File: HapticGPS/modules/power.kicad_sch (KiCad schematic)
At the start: 16 parts, among them U1 NPM1300

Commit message: save
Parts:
- C3: footprint Capacitor_SMD:C_0603_1608Metric -> Capacitor_SMD:C_0402_1005Metric; Number Part GRM188Z71E225ME43D -> GRM155Z71A225KE44D; Voltage 25VDC -> 10V
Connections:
- net SW1_NPM: now reaches L1.1, U1.3 (SW1)
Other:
- moved on the sheet: C1, L1
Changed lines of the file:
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@@
 	)
 	(junction
-		(at 190.5 66.04)
+		(at 196.85 66.04)
 		(diameter 0)
 		(color 0 0 0 0)
@@
 	)
 	(junction
-		(at 180.34 66.04)
+		(at 186.69 66.04)
 		(diameter 0)
 		(color 0 0 0 0)
@@
 	)
 	(junction
-		(at 190.5 78.74)
+		(at 196.85 78.74)
 		(diameter 0)
 		(color 0 0 0 0)
@@
 	(wire
 		(pts
-			(xy 190.5 78.74) (xy 167.64 78.74)
-		)
-		(stroke
-			(width 0)
-			(type default)
-		)
-	)
-	(wire
-		(pts
-			(xy 190.5 66.04) (xy 198.12 66.04)
+			(xy 196.85 66.04) (xy 204.47 66.04)
 		)
 		(stroke
@@
 	(wire
 		(pts
-			(xy 190.5 66.04) (xy 190.5 68.58)
+			(xy 196.85 66.04) (xy 196.85 68.58)
 		)
 		(stroke
@@
 	(wire
 		(pts
+			(xy 167.64 78.74) (xy 196.85 78.74)
+		)
+		(stroke
+			(width 0)
+			(type default)
+		)
+	)
+	(wire
+		(pts
 			(xy 96.52 134.62) (xy 102.87 134.62)
 		)
@@
 	(wire
 		(pts
+			(xy 167.64 66.04) (xy 186.69 66.04)
+		)
+		(stroke
+			(width 0)
+			(type default)
+		)
+	)
+	(wire
+		(pts
 			(xy 115.57 68.58) (xy 127 68.58)
 		)
@@
 	(wire
 		(pts
-			(xy 167.64 76.2) (xy 172.72 76.2)
+			(xy 167.64 76.2) (xy 179.07 76.2)
 		)
 		(stroke
@@
 	(wire
 		(pts
-			(xy 190.5 76.2) (xy 190.5 78.74)
+			(xy 196.85 76.2) (xy 196.85 78.74)
 		)
 		(stroke
@@
 	(wire
 		(pts
-			(xy 180.34 66.04) (xy 190.5 66.04)
+			(xy 186.69 66.04) (xy 196.85 66.04)
 		)
 		(stroke
@@
 	(wire
 		(pts
-			(xy 180.34 66.04) (xy 180.34 76.2)
+			(xy 186.69 66.04) (xy 186.69 76.2)
 		)
 		(stroke
@@
 	(wire
 		(pts
-			(xy 167.64 66.04) (xy 180.34 66.04)
-		)
-		(stroke
-			(width 0)
-			(type default)
-		)
-	)
-	(wire
-		(pts
 			(xy 50.8 53.34) (xy 50.8 48.26)
 		)
@@
 		)
 	)
+	(label "SW1_NPM"
+		(at 167.64 76.2 0)
+		(effects
+			(font
+				(size 1.27 1.27)
+			)
+			(justify left bottom)
+		)
+	)
 	(label "CC2"
 		(at 115.57 44.45 0)
@@
 	(hierarchical_label "BUCK1"
 		(shape output)
-		(at 198.12 66.04 0)
+		(at 204.47 66.04 0)
 		(effects
 			(font
@@
 	(symbol
 		(lib_id "Device:L")
-		(at 176.53 76.2 90)
+		(at 182.88 76.2 90)
 		(unit 1)
 		(exclude_from_sim no)
@@
 		(dnp no)
 		(property "Reference" "L1"
-			(at 176.53 77.47 90)
+			(at 182.88 77.47 90)
 			(effects
 				(font
@@
 		)
 		(property "Value" "2.2uF"
-			(at 176.784 74.168 90)
+			(at 183.134 74.168 90)
 			(effects
 				(font
@@
 		)
 		(property "Footprint" "Inductor_SMD:L_1008_2520Metric"
-			(at 176.53 76.2 0)
+			(at 182.88 76.2 0)
 			(effects
 				(font
@@
 		)
 		(property "Datasheet" "https://mm.digikey.com/Volume0/opasdata/d220001/medias/docus/2542/CIGT252008LM2R2MNE_Spec.pdf"
-			(at 176.53 76.2 0)
+			(at 182.88 76.2 0)
 			(effects
 				(font
@@
 		)
 		(property "Description" "FIXED IND 2.2UH 2A 97 MOHM SMD"
-			(at 176.53 76.2 0)
+			(at 182.88 76.2 0)
 			(effects
 				(font
@@
 		)
 		(property "Manufacturer" "Samsung Electro-Mechanics"
-			(at 176.53 76.2 90)
+			(at 182.88 76.2 90)
 			(effects
 				(font
@@
 		)
 		(property "Number Part" "CIGT252008LM2R2MNE"
-			(at 176.53 76.2 90)
+			(at 182.88 76.2 90)
 			(effects
 				(font
@@
 		)
 		(property "Provider" "Digikey"
-			(at 176.53 76.2 90)
+			(at 182.88 76.2 90)
 			(effects
 				(font
@@
 		)
 		(property "Revisado" "REV"
-			(at 176.53 71.882 90)
+			(at 182.88 71.882 90)
 			(effects
 				(font
@@
 		)
 		(property "Voltage" ""
-			(at 176.53 76.2 0)
+			(at 182.88 76.2 0)
 			(effects
 				(font
@@
 	(symbol
 		(lib_id "power:GND")
-		(at 190.5 78.74 0)
+		(at 196.85 78.74 0)
 		(unit 1)
 		(exclude_from_sim no)
@@
 		(fields_autoplaced yes)
 		(property "Reference" "#PWR07"
-			(at 190.5 85.09 0)
+			(at 196.85 85.09 0)
 			(effects
 				(font
@@
 		)
 		(property "Value" "GND"
-			(at 190.5 83.82 0)
+			(at 196.85 83.82 0)
 			(effects
 				(font
@@
 		)
 		(property "Footprint" ""
-			(at 190.5 78.74 0)
+			(at 196.85 78.74 0)
 			(effects
 				(font
@@
 		)
 		(property "Datasheet" ""
-			(at 190.5 78.74 0)
+			(at 196.85 78.74 0)
 			(effects
 				(font
@@
 		)
 		(property "Description" "Power symbol creates a global label with name \"GND\" , ground"
-			(at 190.5 78.74 0)
+			(at 196.85 78.74 0)
 			(effects
 				(font
@@
 			)
 		)
-		(property "Footprint" "Capacitor_SMD:C_0603_1608Metric"
+		(property "Footprint" "Capacitor_SMD:C_0402_1005Metric"
 			(at 102.5652 49.53 0)
 			(effects
@@
 			)
 		)
-		(property "Datasheet" "https://search.murata.co.jp/Ceramy/image/img/A01X/G101/ENG/GRM188Z71E225ME43-01.pdf"
+		(property "Datasheet" "https://search.murata.co.jp/Ceramy/image/img/A01X/G101/ENG/GRM155Z71A225KE44-01A.pdf"
 			(at 101.6 45.72 0)
 			(effects
@@
 			)
 		)
-		(property "Description" "CAP CER 2.2UF 25V X7R 0603"
+		(property "Description" "CAP CER 2.2UF 10V X7R 0402"
 			(at 101.6 45.72 0)
 			(effects
@@
 			)
 		)
-		(property "Number Part" "GRM188Z71E225ME43D"
+		(property "Number Part" "GRM155Z71A225KE44D"
 			(at 101.6 45.72 0)
 			(effects
@@
 			)
 		)
-		(property "Voltage" "25VDC"
-			(at 108.458 49.276 0)
+		(property "Voltage" "10V"
+			(at 107.442 49.276 0)
 			(effects
 				(font
@@
 	(symbol
 		(lib_id "Device:C")
-		(at 190.5 72.39 0)
+		(at 196.85 72.39 0)
 		(unit 1)
 		(exclude_from_sim no)
@@
 		(dnp no)
 		(property "Reference" "C1"
-			(at 194.31 71.1199 0)
+			(at 200.66 71.1199 0)
 			(effects
 				(font
@@
 		)
 		(property "Value" "10uF"
-			(at 194.31 73.6599 0)
+			(at 200.66 73.6599 0)
 			(effects
 				(font
@@
 		)
 		(property "Footprint" "Capacitor_SMD:C_0603_1608Metric"
-			(at 191.4652 76.2 0)
+			(at 197.8152 76.2 0)
 			(effects
 				(font
@@
 		)
 		(property "Datasheet" "https://search.murata.co.jp/Ceramy/image/img/A01X/G101/ENG/GRM188Z71A106KA73-01A.pdf"
-			(at 190.5 72.39 0)
+			(at 196.85 72.39 0)
 			(effects
 				(font
@@
 		)
 		(property "Description" "CAP CER 10UF 10V X7R 0603"
-			(at 190.5 72.39 0)
+			(at 196.85 72.39 0)
 			(effects
 				(font
@@
 		)
 		(property "Manufacturer" "Murata Electronics"
-			(at 190.5 72.39 0)
+			(at 196.85 72.39 0)
 			(effects
 				(font
@@
 		)
 		(property "Number Part" "GRM188Z71A106KA73D"
-			(at 190.5 72.39 0)
+			(at 196.85 72.39 0)
 			(effects
 				(font
@@
 		)
 		(property "Provider" "Digikey"
-			(at 190.5 72.39 0)
+			(at 196.85 72.39 0)
 			(effects
 				(font
@@
 		)
 		(property "Voltage" "10V"
-			(at 196.088 75.946 0)
+			(at 202.438 75.946 0)
 			(effects
 				(font
@@
 		)
 		(property "Revisado" "REV"
-			(at 196.088 78.232 0)
+			(at 202.438 78.232 0)
 			(effects
 				(font

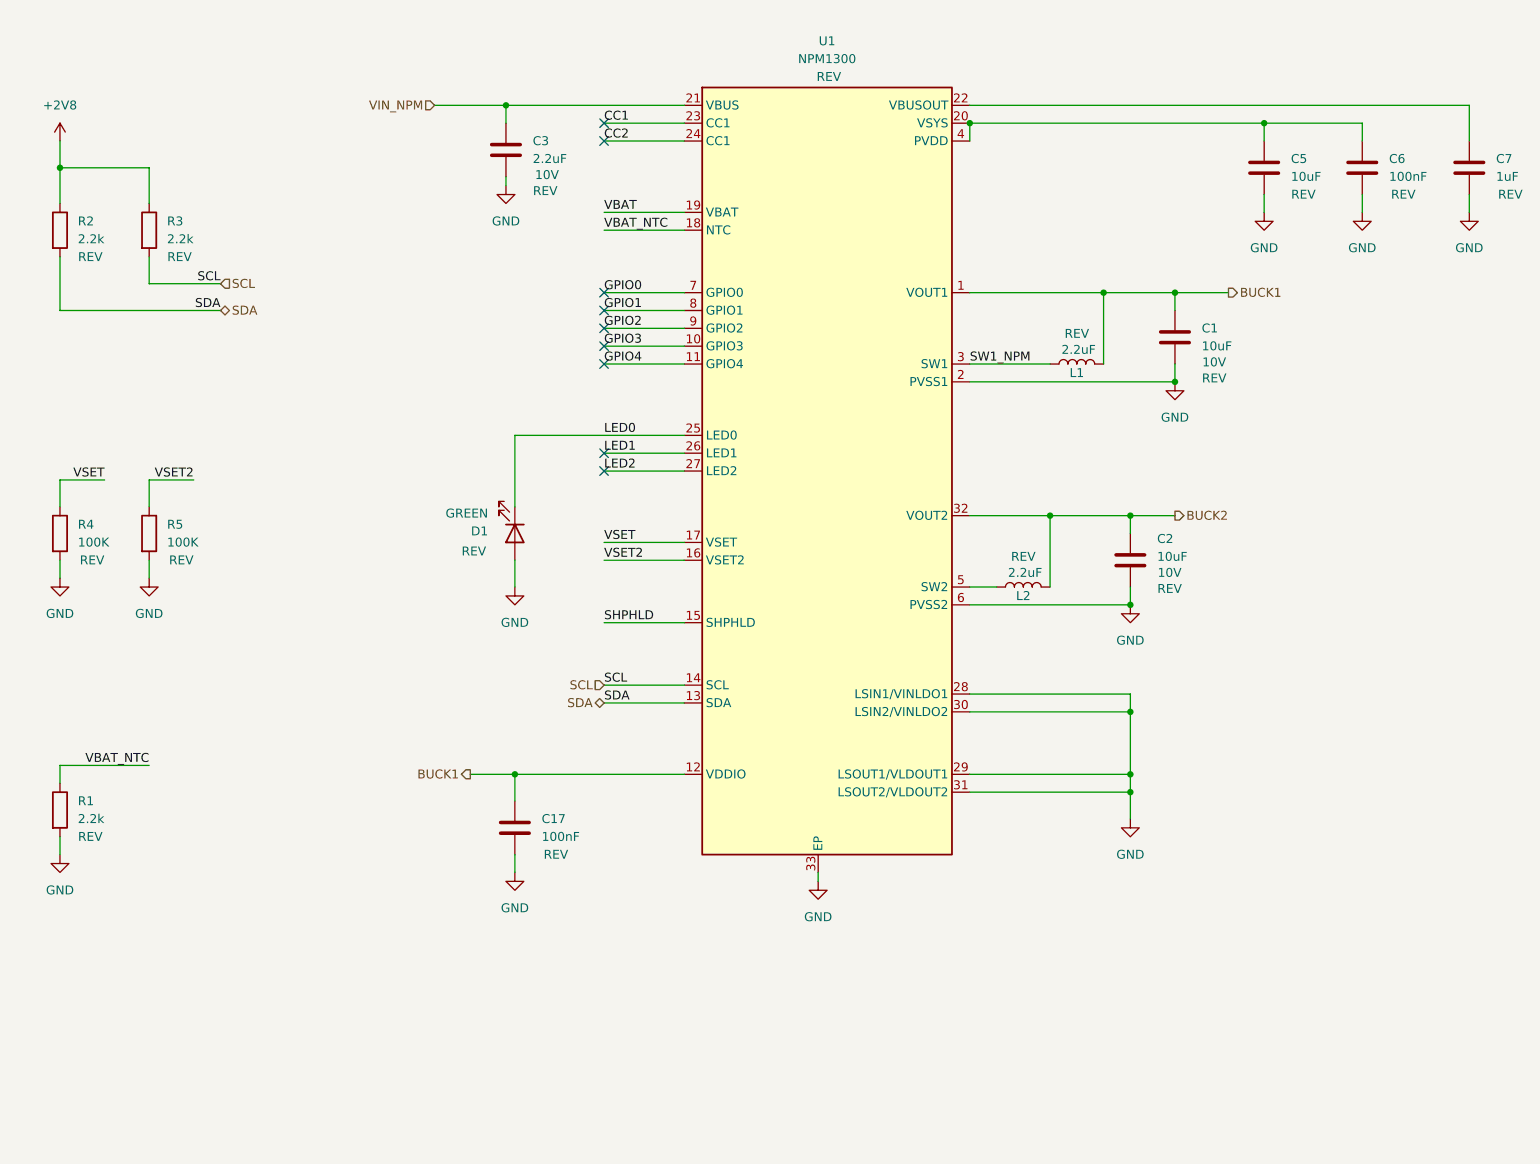
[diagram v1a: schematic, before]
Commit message: eliminating GPS, and second piezo driver
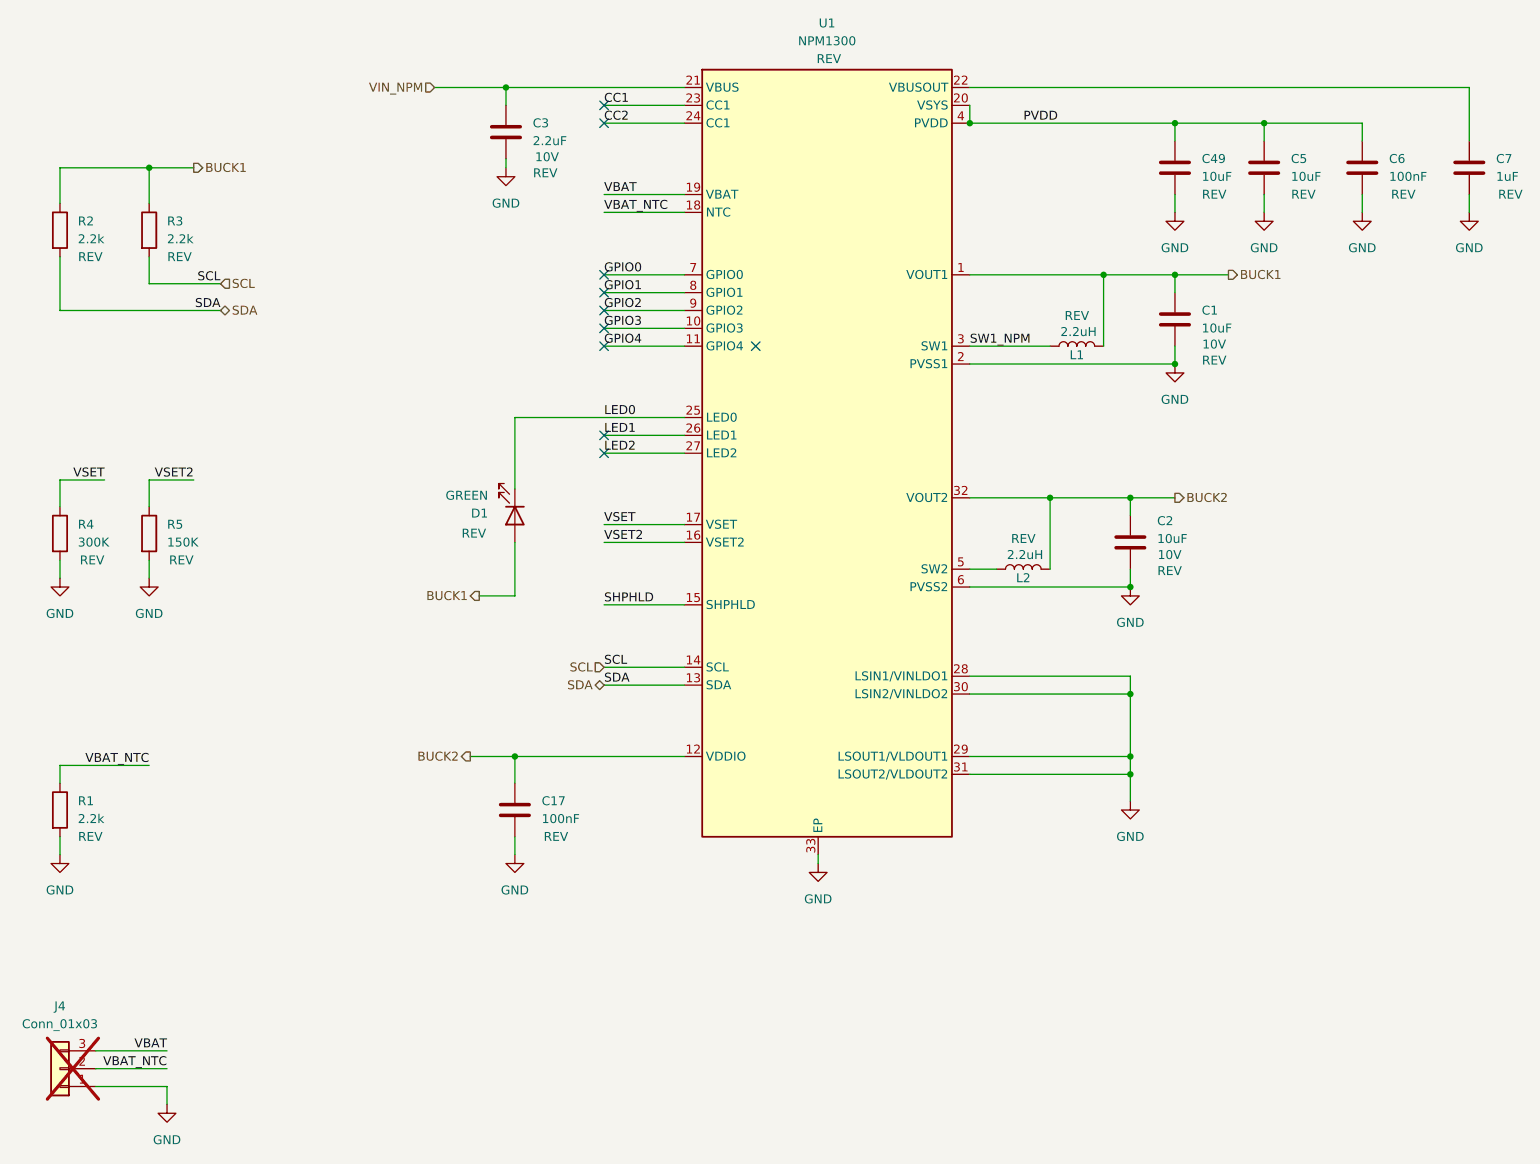
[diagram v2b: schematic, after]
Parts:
- added C49: 10uF, Capacitor_SMD:C_0603_1608Metric, symbol Device:C
- added J4: Conn_01x03, Solderpads:01x03_1.5x3, symbol Connector_Generic:Conn_01x03
- C17, C6: footprint Capacitor_SMD:C_0603_1608Metric -> Capacitor_SMD:C_0402_1005Metric; Manufacturer KEMET -> Murata Electronics; Number Part C0603C104K3RACTU -> GCM155R71H104KE02J
- C5: footprint Capacitor_SMD:C_0805_2012Metric -> Capacitor_SMD:C_0603_1608Metric; Number Part GRM21BZ71E106KE15L -> GRM188Z71A106KA73D
- C7: footprint Capacitor_SMD:C_0603_1608Metric -> Capacitor_SMD:C_0402_1005Metric; Manufacturer Digikey -> Murata Electronics; Number Part C0603C105K4RACTU -> GRM155R61C105KA12D
- L1, L2: value 2.2uF -> 2.2uH
- R1, R2, R3: footprint Capacitor_SMD:C_0603_1608Metric -> Resistor_SMD:R_0603_1608Metric
- R4: value 100K -> 300K; footprint Resistor_SMD:R_0603_1608Metric -> Resistor_SMD:R_0402_1005Metric; Number Part RC0603FR-07100KL -> RC0402FR-07300KL
- R5: value 100K -> 150K; footprint Resistor_SMD:R_0603_1608Metric -> Resistor_SMD:R_0402_1005Metric; Manufacturer YAGEO -> TE Connectivity Passive Product; Number Part RC0603FR-07100KL -> CPF0402B150KE1
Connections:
- net +2V8 is gone; now on net BUCK1: R2.1, R3.1
- net BUCK1: now also D1.2 (A); no longer C17.1, U1.12 (VDDIO)
- net BUCK2: now also C17.1, U1.12 (VDDIO)
- net GND: now also C49.2, J4.1 (Pin_1); no longer D1.2 (A)
- net VBAT: now also J4.3 (Pin_3)
- net VBAT_NTC: now also J4.2 (Pin_2)
- net PVDD: now reaches C5.1, C6.1, U1.20 (VSYS), U1.4 (PVDD)
- net PVDD: now also C49.1
- no-connect marks 9 -> 10
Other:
- moved on the sheet: C1, C2, C3, D1, L1, L2, U1
